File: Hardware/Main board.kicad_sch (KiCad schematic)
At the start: 39 parts, among them J1 RBUS, U1 ESP32-S3, Y1 R940000171

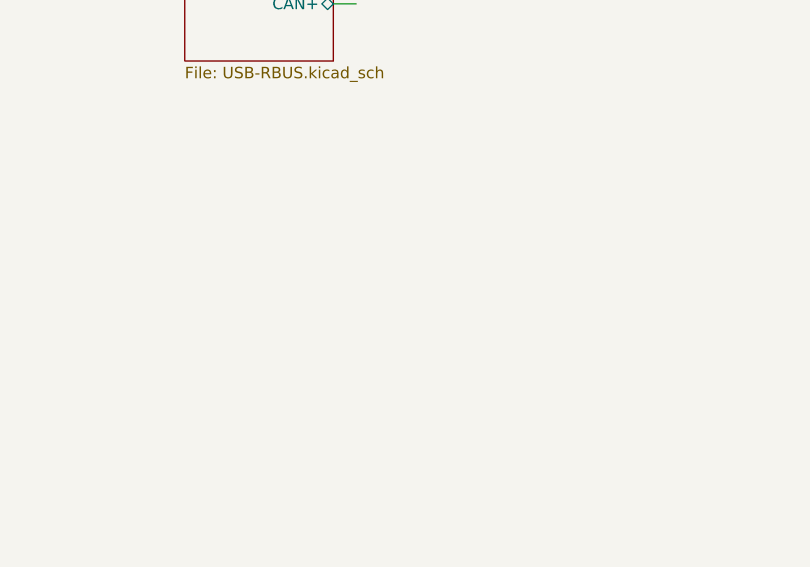
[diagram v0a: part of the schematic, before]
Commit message: New Buck boost converter
+ new sorted circuit, voltage regulation not finalised
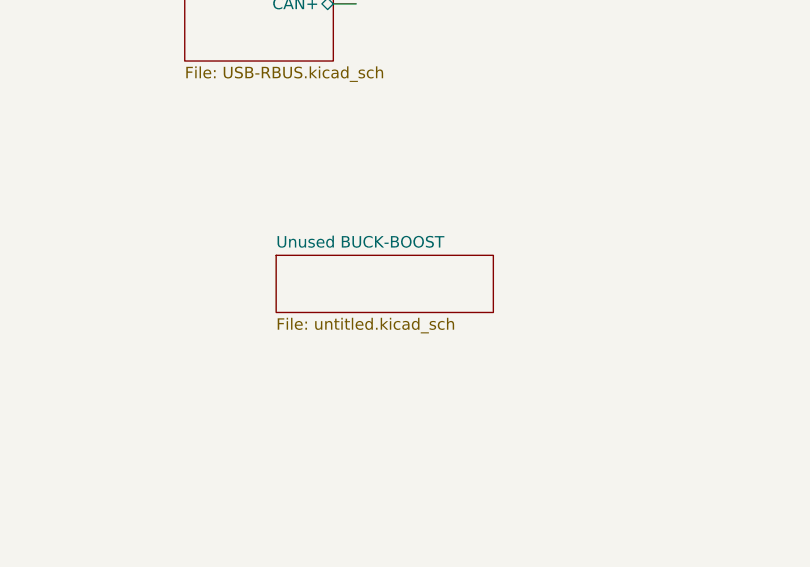
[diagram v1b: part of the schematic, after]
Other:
- added sheet Unused BUCK-BOOST (untitled.kicad_sch)
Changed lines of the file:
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@@
+	)
+	(sheet
+		(at 213.36 153.67)
+		(size 24.13 6.35)
+		(fields_autoplaced yes)
+		(stroke
+			(width 0.1524)
+			(type solid)
+		)
+		(fill
+			(color 0 0 0 0.0000)
+		)
+		(property "Sheetname" "Unused BUCK-BOOST"
+			(at 213.36 152.9584 0)
+			(effects
+				(font
+					(size 1.27 1.27)
+				)
+				(justify left bottom)
+			)
+		)
+		(property "Sheetfile" "untitled.kicad_sch"
+			(at 213.36 160.6046 0)
+			(effects
+				(font
+					(size 1.27 1.27)
+				)
+				(justify left top)
+			)
+		)
+		(instances
+			(project "Main board"
+				(path "/7db990e4-92e1-4f99-b4d2-435bbec1ba83"
+					(page "9")
+				)
+			)
+		)
 	)
 	(sheet

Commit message: PCB mid design
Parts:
- removed J1: RBUS, Connector_Molex:Molex_Mini-Fit_Jr_5566-06A_2x03_P4.20mm_Vertical, symbol Connector:Conn_01x06_Male
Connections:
- net Chip_Selec: now also U1.38 (GPIO33); no longer U1.19 (GPIO14/ADC2_CH3)
- net Cont 1: now also U1.43 (GPIO38); no longer U1.42 (GPIO37)
- net Interrupt : now also U1.17 (GPIO12/ADC2_CH1); no longer U1.44 (MTCK/JTAG/GPIO39)
- net MISO: now also U1.41 (GPIO36); no longer U1.39 (GPIO34)
- net MOSI: now also U1.39 (GPIO34); no longer U1.38 (GPIO33)
- net Nuke 1: now also U1.42 (GPIO37); no longer U1.41 (GPIO36)
- net SCL_I2C: now also U1.19 (GPIO14/ADC2_CH3); no longer U1.43 (GPIO38)
- net SDA-CS: now also U1.44 (MTCK/JTAG/GPIO39); no longer U1.18 (GPIO13/ADC2_CH2)
- net SDA-Photo: now also U1.18 (GPIO13/ADC2_CH2); no longer U1.17 (GPIO12/ADC2_CH1)
- net SDA-BuckBC: now reaches U1.10 (GPIO5/ADC1_CH4)
- net INT: now reaches U1.11 (GPIO6/ADC1_CH5)
- net SD1_DET: now reaches U1.12 (GPIO7/ADC1_CH6)
- net VSPI_MOSI: now reaches U1.13 (GPIO8/ADC1_CH7)
- net SD1_CS: now reaches U1.14 (GPIO9/ADC1_CH8)
- net VSPI_SCLK: now reaches U1.15 (GPIO10/ADC1_CH9)
- net VSPI_MISO: now reaches U1.16 (GPIO11/ADC2_CH0)
- net PG: no longer names the net of U1.27 (GPIO21)
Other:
- removed sheet Unused BUCK-BOOST
- added sheet SD-card (SD.kicad_sch)
- sheet Voltage Regulation ports: added INT_Fault, SDA-BuckBC; removed PWR-GD

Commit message: PCB done more ish
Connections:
- net SD1_CS: now also U1.13 (GPIO8/ADC1_CH7); no longer U1.14 (GPIO9/ADC1_CH8)
- net VSPI_MOSI: now also U1.14 (GPIO9/ADC1_CH8); no longer U1.13 (GPIO8/ADC1_CH7)
- net CC: no longer names the net of U1.48 (MTMS/JTAG/GPIO42)
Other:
- sheet Voltage Regulation ports: added none; removed CC
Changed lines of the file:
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@@
 	(wire
 		(pts
-			(xy 237.49 52.07) (xy 236.22 52.07)
-		)
-		(stroke
-			(width 0)
-			(type default)
-		)
-	)
-	(wire
-		(pts
 			(xy 39.37 30.48) (xy 39.37 40.64)
 		)
@@
 	(wire
 		(pts
-			(xy 67.31 125.73) (xy 69.85 125.73)
-		)
-		(stroke
-			(width 0)
-			(type default)
-		)
-	)
-	(wire
-		(pts
 			(xy 73.66 26.67) (xy 71.12 26.67)
 		)
@@
 		)
 	)
-	(label "CC"
-		(at 237.49 52.07 0)
+	(label "Chip_Selec"
+		(at 201.93 85.09 180)
 		(fields_autoplaced yes)
 		(effects
@@
 				(size 1.27 1.27)
 			)
-			(justify left bottom)
+			(justify right bottom)
 		)
 	)
-	(label "Chip_Selec"
-		(at 201.93 85.09 180)
+	(label "VSPI_MOSI"
+		(at 62.23 92.71 180)
 		(fields_autoplaced yes)
 		(effects
@@
 		)
 	)
-	(label "CC"
-		(at 67.31 125.73 180)
-		(fields_autoplaced yes)
-		(effects
-			(font
-				(size 1.27 1.27)
-			)
-			(justify right bottom)
-		)
-	)
 	(label "SCK_Baro"
 		(at 139.7 100.33 0)
@@
 	)
 	(label "VSPI_MOSI"
-		(at 62.23 90.17 180)
-		(fields_autoplaced yes)
-		(effects
-			(font
-				(size 1.27 1.27)
-			)
-			(justify right bottom)
-		)
-	)
-	(label "VSPI_MOSI"
 		(at 262.89 146.05 180)
 		(fields_autoplaced yes)
@@
 		)
 	)
-	(label "SD1_CS"
-		(at 62.23 92.71 180)
-		(fields_autoplaced yes)
-		(effects
-			(font
-				(size 1.27 1.27)
-			)
-			(justify right bottom)
-		)
-	)
 	(label "BOOT"
 		(at 68.58 165.1 180)
@@
 		)
 	)
+	(label "SD1_CS"
+		(at 62.23 90.17 180)
+		(fields_autoplaced yes)
+		(effects
+			(font
+				(size 1.27 1.27)
+			)
+			(justify right bottom)
+		)
+	)
 	(label "CAN-"
 		(at 115.57 187.96 0)
@@
 			)
 		)
-		(pin "CC" output
-			(at 236.22 52.07 0)
-			(effects
-				(font
-					(size 1.27 1.27)
-				)
-				(justify right)
-			)
-		)

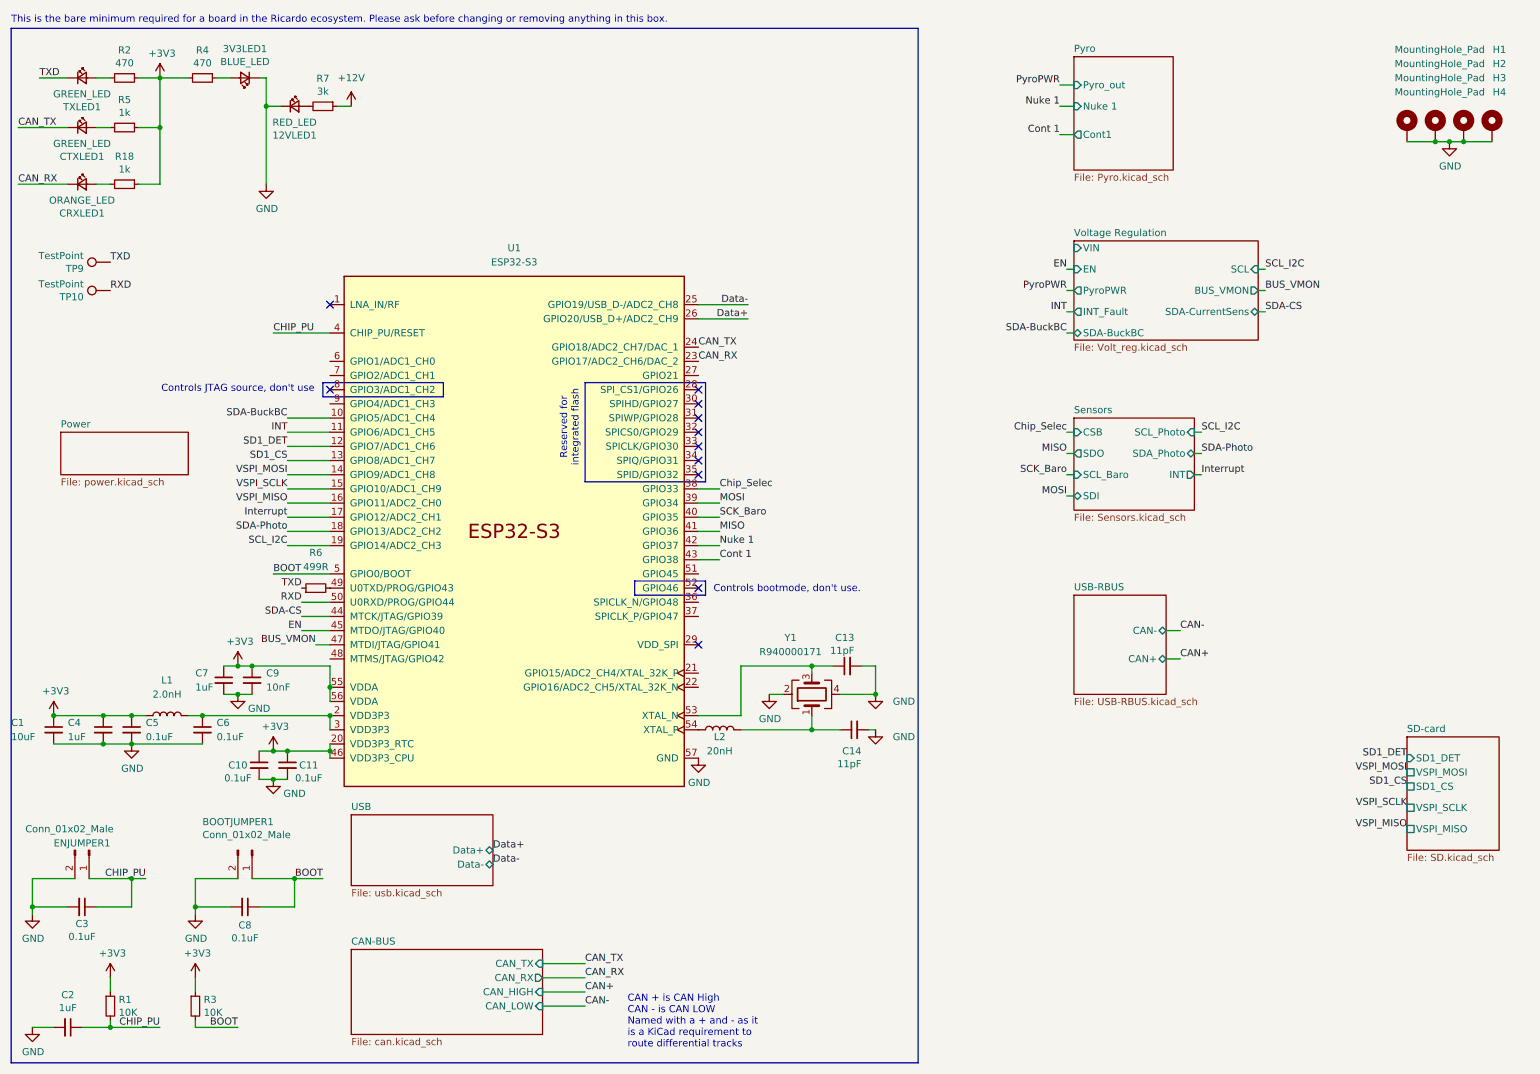
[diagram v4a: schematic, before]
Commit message: SD card fix + logos
Changed SD card from the lock in to the push in
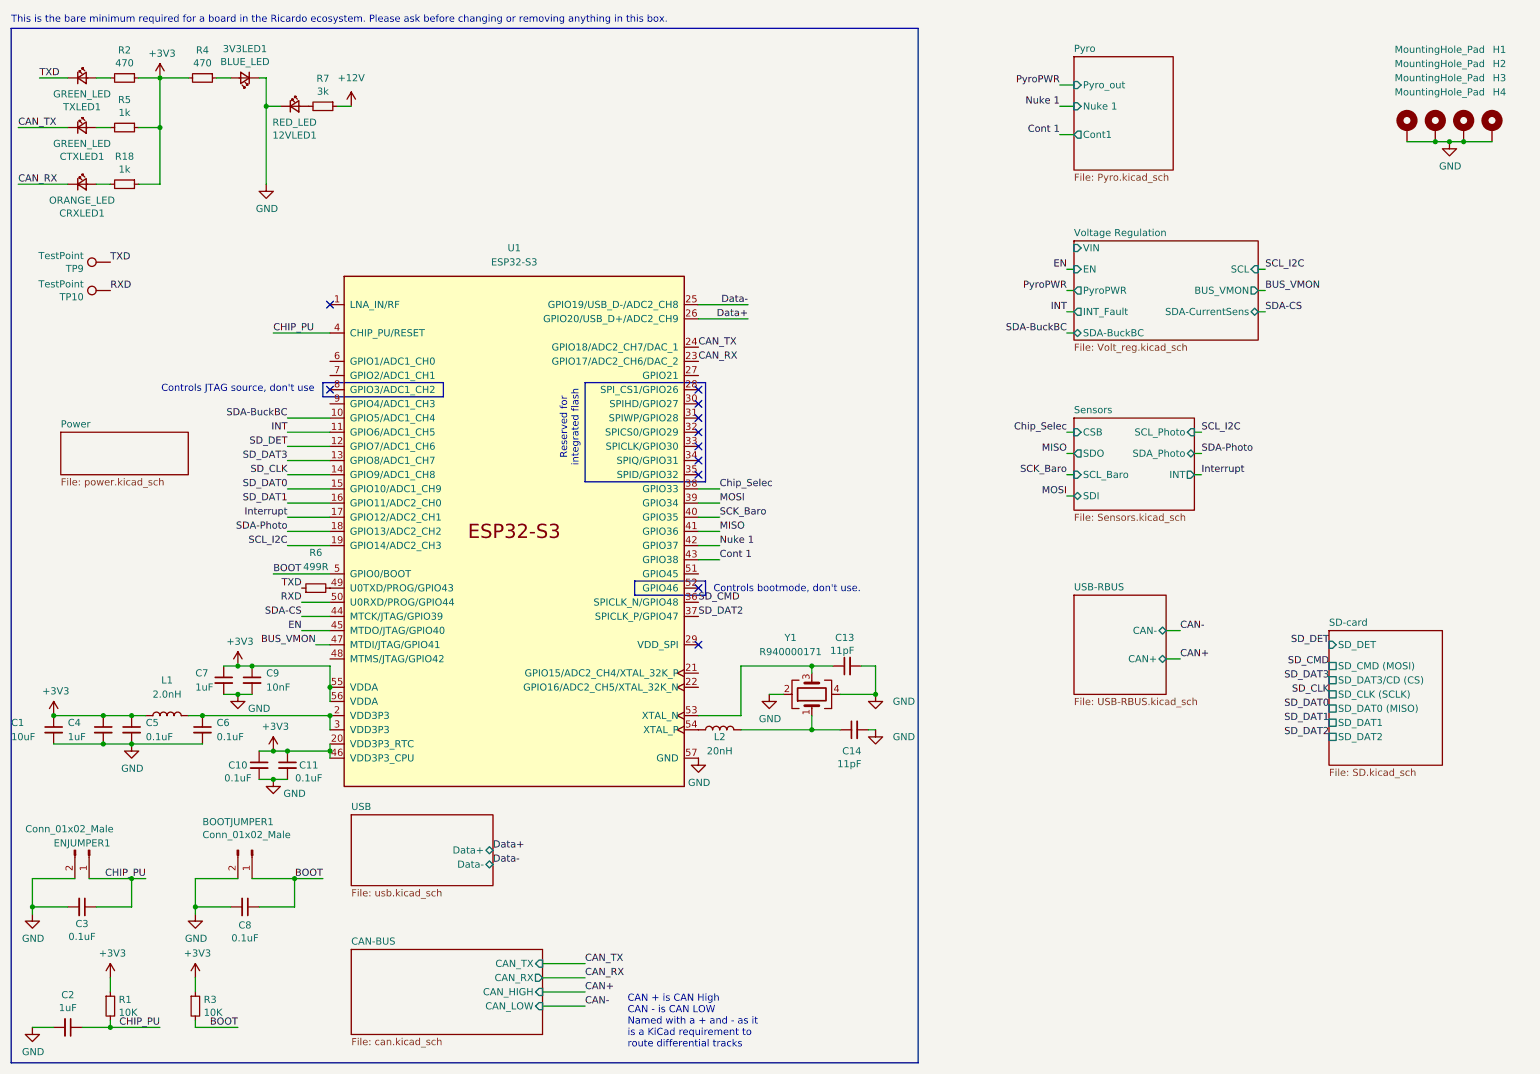
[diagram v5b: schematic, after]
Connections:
- net SD_CMD: now reaches U1.36 (SPICLK_N/GPIO48)
- net SD_DAT2: now reaches U1.37 (SPICLK_P/GPIO47)
- net SD1_CS renamed SD_DAT3
- net SD1_DET renamed SD_DET
- net VSPI_MISO renamed SD_DAT1
- net VSPI_MOSI renamed SD_CLK
- net VSPI_SCLK renamed SD_DAT0
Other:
- sheet SD-card ports: added SD_CLK (SCLK), SD_CMD (MOSI), SD_DAT0 (MISO), SD_DAT1, SD_DAT2, SD_DAT3/CD (CS), SD_DET; removed SD1_CS, SD1_DET, VSPI_MISO, VSPI_MOSI, VSPI_SCLK
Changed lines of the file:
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@@
 		)
 	)
-	(label "VSPI_MOSI"
-		(at 62.23 92.71 180)
+	(label "SD_CLK"
+		(at 248.92 132.08 180)
 		(effects
 			(font
@@
 		)
 	)
-	(label "VSPI_SCLK"
-		(at 262.89 152.4 180)
+	(label "SD_DAT1"
+		(at 248.92 137.16 180)
 		(effects
 			(font
@@
 		)
 	)
-	(label "VSPI_MISO"
-		(at 62.23 97.79 180)
-		(effects
-			(font
-				(size 1.27 1.27)
-			)
-			(justify right bottom)
-		)
-	)
 	(label "SCL_I2C"
 		(at 226.06 85.09 0)
@@
 		)
 	)
-	(label "VSPI_SCLK"
-		(at 62.23 95.25 180)
+	(label "SD_CMD"
+		(at 248.92 127 180)
 		(effects
 			(font
@@
 		)
 	)
-	(label "VSPI_MOSI"
-		(at 262.89 146.05 180)
+	(label "SCK_Baro"
+		(at 201.93 92.71 180)
 		(effects
 			(font
@@
 		)
 	)
-	(label "SCK_Baro"
-		(at 201.93 92.71 180)
+	(label "SD_DAT3"
+		(at 62.23 90.17 180)
 		(effects
 			(font
@@
 		)
 	)
+	(label "SD_CMD"
+		(at 135.89 115.57 0)
+		(effects
+			(font
+				(size 1.27 1.27)
+			)
+			(justify left bottom)
+		)
+	)
 	(label "MISO"
 		(at 201.93 88.9 180)
@@
 		)
 	)
-	(label "VSPI_MISO"
-		(at 262.89 156.21 180)
+	(label "SD_DAT2"
+		(at 135.89 118.11 0)
+		(effects
+			(font
+				(size 1.27 1.27)
+			)
+			(justify left bottom)
+		)
+	)
+	(label "SD_DAT0"
+		(at 248.92 134.62 180)
 		(effects
 			(font
@@
 		)
 	)
+	(label "SD_DAT1"
+		(at 62.23 97.79 180)
+		(effects
+			(font
+				(size 1.27 1.27)
+			)
+			(justify right bottom)
+		)
+	)
 	(label "INT"
 		(at 62.23 85.09 180)
@@
 		)
 	)
-	(label "SD1_DET"
-		(at 62.23 87.63 180)
+	(label "SD_CLK"
+		(at 62.23 92.71 180)
+		(effects
+			(font
+				(size 1.27 1.27)
+			)
+			(justify right bottom)
+		)
+	)
+	(label "SD_DAT0"
+		(at 62.23 95.25 180)
 		(effects
 			(font
@@
 		)
 	)
+	(label "SD_DAT2"
+		(at 248.92 139.7 180)
+		(effects
+			(font
+				(size 1.27 1.27)
+			)
+			(justify right bottom)
+		)
+	)
 	(label "RXD"
 		(at 64.77 115.57 180)
@@
 		)
 	)
-	(label "SD1_DET"
-		(at 262.89 143.51 180)
+	(label "SD_DET"
+		(at 248.92 123.19 180)
 		(effects
 			(font
@@
 		)
 	)
+	(label "SD_DET"
+		(at 62.23 87.63 180)
+		(effects
+			(font
+				(size 1.27 1.27)
+			)
+			(justify right bottom)
+		)
+	)
 	(label "CAN_RX"
 		(at 135.89 72.39 0)
@@
 		)
 	)
-	(label "SD1_CS"
-		(at 62.23 90.17 180)
-		(effects
-			(font
-				(size 1.27 1.27)
-			)
-			(justify right bottom)
-		)
-	)
 	(label "CAN-"
 		(at 115.57 187.96 0)
@@
 		)
 	)
-	(label "SD1_CS"
-		(at 262.89 148.59 180)
+	(label "SD_DAT3"
+		(at 248.92 129.54 180)
 		(effects
 			(font
@@
 	)
 	(sheet
-		(at 262.89 139.7)
-		(size 16.51 20.32)
+		(at 248.92 120.65)
+		(size 20.32 24.13)
 		(exclude_from_sim no)
 		(in_bom yes)
@@
 		)
 		(property "Sheetname" "SD-card"
-			(at 262.89 138.9884 0)
+			(at 248.92 119.9384 0)
 			(effects
 				(font
@@
 		)
 		(property "Sheetfile" "SD.kicad_sch"
-			(at 262.89 160.6046 0)
+			(at 248.92 145.3646 0)
 			(effects
 				(font
@@
 			)
 		)
-		(pin "SD1_DET" input
-			(at 262.89 143.51 180)
+		(pin "SD_DAT3{slash}CD (CS)" passive
+			(at 248.92 129.54 180)
+			(effects
+				(font
+					(size 1.27 1.27)
+				)
+				(justify left)
+			)
+		)
+		(pin "SD_CMD (MOSI)" passive
+			(at 248.92 127 180)
+			(effects
+				(font
+					(size 1.27 1.27)
+				)
+				(justify left)
+			)
+		)
+		(pin "SD_CLK (SCLK)" passive
+			(at 248.92 132.08 180)
 			(effects
 				(font
@@
 			)
 		)
-		(pin "SD1_CS" passive
-			(at 262.89 148.59 180)
+		(pin "SD_DAT0 (MISO)" passive
+			(at 248.92 134.62 180)
 			(effects
 				(font
@@
 			)
 		)
-		(pin "VSPI_MOSI" passive
-			(at 262.89 146.05 180)
+		(pin "SD_DAT1" passive
+			(at 248.92 137.16 180)
 			(effects
 				(font
@@
 			)
 		)
-		(pin "VSPI_SCLK" passive
-			(at 262.89 152.4 180)
+		(pin "SD_DET" input
+			(at 248.92 123.19 180)
 			(effects
 				(font
@@
 			)
 		)
-		(pin "VSPI_MISO" passive
-			(at 262.89 156.21 180)
+		(pin "SD_DAT2" passive
+			(at 248.92 139.7 180)
 			(effects
 				(font

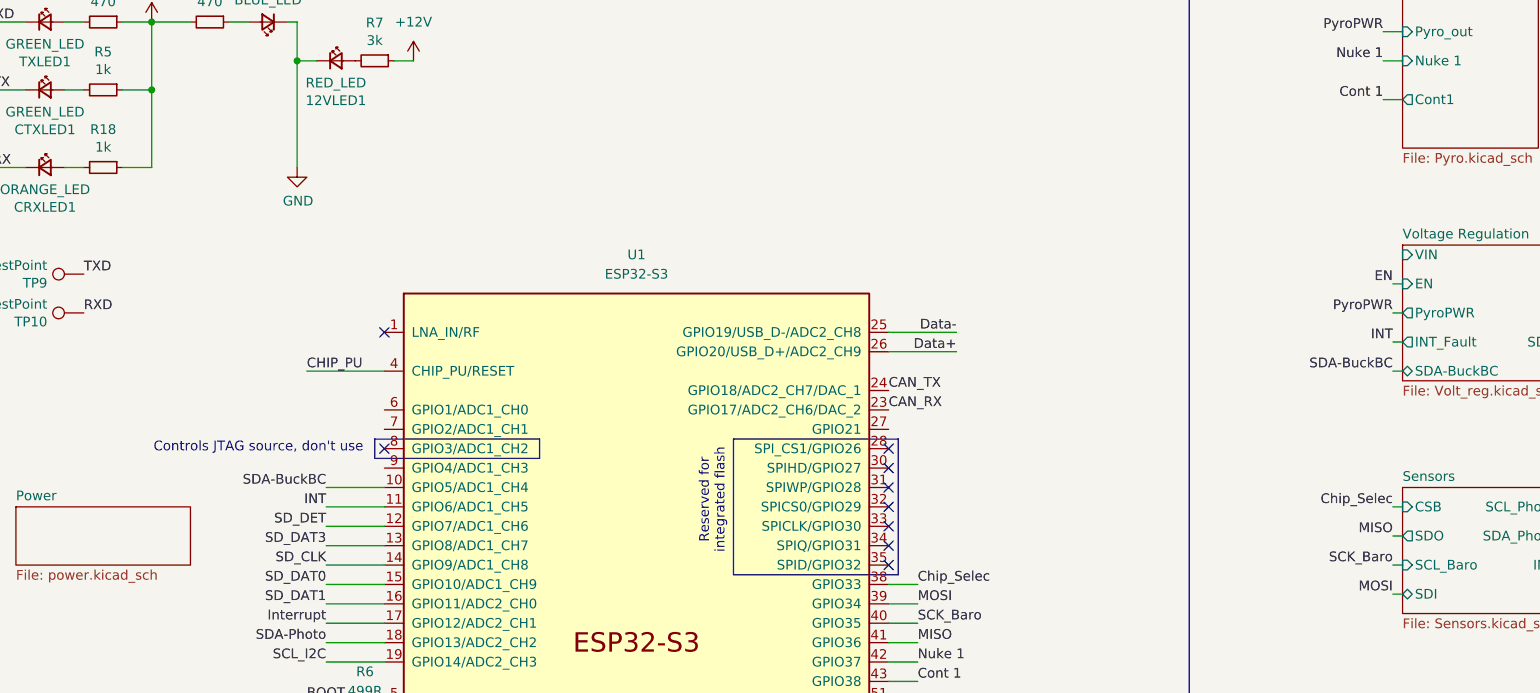
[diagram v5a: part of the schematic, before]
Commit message: Swapped battery & nichrome positions
fixed crystal and other small things
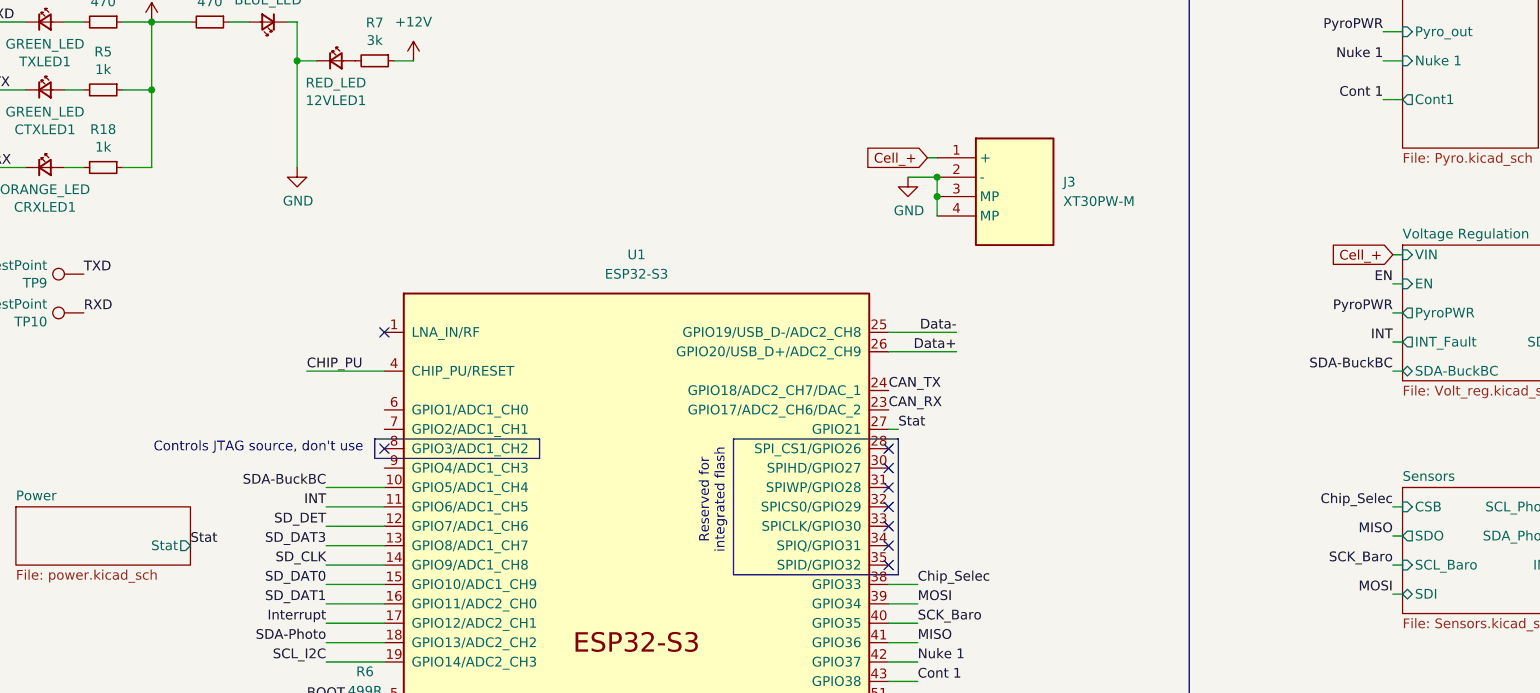
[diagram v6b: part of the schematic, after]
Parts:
- added J3: XT30PW-M, iclr:XT30PWM, symbol iclr:XT30PW-M
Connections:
- net GND: now also J3.2 (-), J3.3 (MP), J3.4 (MP)
- net Stat: now reaches U1.27 (GPIO21)
- new net Cell_+: J3.1 (+)
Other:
- sheet Power ports: added Stat; removed none
